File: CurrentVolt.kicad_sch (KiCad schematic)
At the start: 6 parts, among them U13 ACS70331EOLCTR-2P5U3, U14 Opamp_Dual

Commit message: finalising diagram
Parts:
- removed R24, R25: R, symbol Device:R
- removed U14: Opamp_Dual, symbol Device:Opamp_Dual
- renumbered R14 to R22, R15 to R23, U13 to U14
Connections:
- net +3.3V renamed 3v3
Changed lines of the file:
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@@
 (kicad_sch (version 20211123) (generator eeschema)
   (paper "A4")
-  (junction (at 171.45 110.49) (diameter 0) (color 0 0 0 0)
-  )
-  (junction (at 116.84 96.52) (diameter 0) (color 0 0 0 0)
+  (junction (at 116.84 91.44) (diameter 0) (color 0 0 0 0)
   )
   (junction (at 116.84 105.41) (diameter 0) (color 0 0 0 0)
-  )
-  (junction (at 156.21 113.03) (diameter 0) (color 0 0 0 0)
   )
   (junction (at 116.84 114.3) (diameter 0) (color 0 0 0 0)
   )
   (junction (at 83.82 81.28) (diameter 0) (color 0 0 0 0)
-  )
-  (junction (at 130.81 105.41) (diameter 0) (color 0 0 0 0)
   )
   (wire (pts (xy 80.01 81.28) (xy 83.82 81.28))
@@
     (stroke (width 0) (type default) (color 0 0 0 0))
   )
-  (wire (pts (xy 82.55 96.52) (xy 86.36 96.52))
+  (wire (pts (xy 116.84 91.44) (xy 116.84 96.52))
     (stroke (width 0) (type default) (color 0 0 0 0))
   )
-  (wire (pts (xy 171.45 110.49) (xy 171.45 120.65))
+  (wire (pts (xy 71.12 96.52) (xy 86.36 96.52))
     (stroke (width 0) (type default) (color 0 0 0 0))
   )
@@
     (stroke (width 0) (type default) (color 0 0 0 0))
   )
-  (wire (pts (xy 116.84 91.44) (xy 116.84 96.52))
-    (stroke (width 0) (type default) (color 0 0 0 0))
-  )
-  (wire (pts (xy 130.81 105.41) (xy 130.81 129.54))
-    (stroke (width 0) (type default) (color 0 0 0 0))
-  )
-  (wire (pts (xy 116.84 88.9) (xy 133.35 88.9))
-    (stroke (width 0) (type default) (color 0 0 0 0))
-  )
   (wire (pts (xy 71.12 91.44) (xy 86.36 91.44))
-    (stroke (width 0) (type default) (color 0 0 0 0))
-  )
-  (wire (pts (xy 130.81 105.41) (xy 156.21 105.41))
     (stroke (width 0) (type default) (color 0 0 0 0))
   )
@@
     (stroke (width 0) (type default) (color 0 0 0 0))
   )
-  (wire (pts (xy 163.83 120.65) (xy 156.21 120.65))
-    (stroke (width 0) (type default) (color 0 0 0 0))
-  )
-  (wire (pts (xy 171.45 107.95) (xy 171.45 110.49))
-    (stroke (width 0) (type default) (color 0 0 0 0))
-  )
-  (wire (pts (xy 116.84 105.41) (xy 130.81 105.41))
-    (stroke (width 0) (type default) (color 0 0 0 0))
-  )
-  (wire (pts (xy 156.21 120.65) (xy 156.21 113.03))
+  (wire (pts (xy 116.84 105.41) (xy 162.56 105.41))
     (stroke (width 0) (type default) (color 0 0 0 0))
   )
@@
     (stroke (width 0) (type default) (color 0 0 0 0))
   )
-  (wire (pts (xy 116.84 96.52) (xy 162.56 96.52))
-    (stroke (width 0) (type default) (color 0 0 0 0))
-  )
-  (wire (pts (xy 130.81 129.54) (xy 171.45 129.54))
-    (stroke (width 0) (type default) (color 0 0 0 0))
-  )
-  (wire (pts (xy 156.21 110.49) (xy 156.21 113.03))
-    (stroke (width 0) (type default) (color 0 0 0 0))
-  )
-  (wire (pts (xy 142.24 113.03) (xy 148.59 113.03))
+  (wire (pts (xy 116.84 91.44) (xy 162.56 91.44))
     (stroke (width 0) (type default) (color 0 0 0 0))
   )
@@
     (stroke (width 0) (type default) (color 0 0 0 0))
   )
-  (wire (pts (xy 171.45 110.49) (xy 173.99 110.49))
-    (stroke (width 0) (type default) (color 0 0 0 0))
-  )
   (wire (pts (xy 116.84 107.95) (xy 116.84 105.41))
     (stroke (width 0) (type default) (color 0 0 0 0))
   )
-  (wire (pts (xy 133.35 78.74) (xy 133.35 88.9))
+  (wire (pts (xy 116.84 88.9) (xy 162.56 88.9))
     (stroke (width 0) (type default) (color 0 0 0 0))
   )
-  (label "GND_0" (at 116.84 115.57 270)
+  (label "GND" (at 116.84 115.57 270)
     (effects (font (size 1.27 1.27)) (justify right bottom))
   )
-  (label "GND_0" (at 80.01 81.28 180)
+  (label "GND" (at 80.01 81.28 180)
     (effects (font (size 1.27 1.27)) (justify right bottom))
   )
-  (label "GND_0" (at 142.24 113.03 180)
-    (effects (font (size 1.27 1.27)) (justify right bottom))
+  (hierarchical_label "3v3" (shape input) (at 71.12 96.52 180)
+    (effects (font (size 1.27 1.27)) (justify right))
   )
   (hierarchical_label "GND" (shape input) (at 66.04 114.3 180)
     (effects (font (size 1.27 1.27)) (justify right))
   )
-  (hierarchical_label "Vin" (shape input) (at 133.35 78.74 90)
+  (hierarchical_label "Vin" (shape input) (at 162.56 88.9 0)
     (effects (font (size 1.27 1.27)) (justify left))
   )
-  (hierarchical_label "Vinv" (shape input) (at 173.99 110.49 0)
+  (hierarchical_label "Vsense" (shape input) (at 162.56 105.41 0)
     (effects (font (size 1.27 1.27)) (justify left))
   )
@@
     (effects (font (size 1.27 1.27)) (justify right))
   )
-  (hierarchical_label "Vsense" (shape input) (at 171.45 129.54 0)
+  (hierarchical_label "Out V" (shape input) (at 162.56 91.44 0)
     (effects (font (size 1.27 1.27)) (justify left))
-  )
-  (hierarchical_label "Out V" (shape input) (at 162.56 96.52 0)
-    (effects (font (size 1.27 1.27)) (justify left))
-  )
-  (symbol (lib_id "Device:Opamp_Dual") (at 163.83 107.95 0) (mirror x) (unit 1)
-    (in_bom yes) (on_board yes) (fields_autoplaced)
-    (property "Reference" "U14" (id 0) (at 163.83 99.1702 0))
-    (property "Value" "Opamp_Dual" (id 1) (at 163.83 101.7071 0))
-    (property "Footprint" "" (id 2) (at 163.83 107.95 0)
-      (effects (font (size 1.27 1.27)) hide)
-    )
-    (property "Datasheet" "~" (id 3) (at 163.83 107.95 0)
-      (effects (font (size 1.27 1.27)) hide)
-    )
-    (pin "1")
-    (pin "2")
-    (pin "3")
-    (pin "5")
-    (pin "6")
-    (pin "7")
-    (pin "4")
-    (pin "8")
   )
   (symbol (lib_id "Device:R_Small") (at 116.84 99.06 0) (unit 1)
     (in_bom yes) (on_board yes) (fields_autoplaced)
-    (property "Reference" "R14" (id 0) (at 118.3386 98.2253 0)
+    (property "Reference" "R22" (id 0) (at 118.3386 98.2253 0)
       (effects (font (size 1.27 1.27)) (justify left))
     )
@@
     (pin "2")
   )
-  (symbol (lib_id "Device:R") (at 152.4 113.03 90) (unit 1)
+  (symbol (lib_id "power:PWR_FLAG") (at 83.82 81.28 0) (unit 1)
     (in_bom yes) (on_board yes) (fields_autoplaced)
-    (property "Reference" "R24" (id 0) (at 152.4 108.3142 90))
-    (property "Value" "R" (id 1) (at 152.4 110.8511 90))
-    (property "Footprint" "" (id 2) (at 152.4 114.808 90)
+    (property "Reference" "#FLG08" (id 0) (at 83.82 79.375 0)
       (effects (font (size 1.27 1.27)) hide)
     )
-    (property "Datasheet" "~" (id 3) (at 152.4 113.03 0)
+    (property "Value" "PWR_FLAG" (id 1) (at 83.82 77.7042 0)
       (effects (font (size 1.27 1.27)) hide)
     )
-    (pin "1")
-    (pin "2")
-  )
-  (symbol (lib_id "power:+3.3V") (at 82.55 96.52 90) (unit 1)
-    (in_bom yes) (on_board yes) (fields_autoplaced)
-    (property "Reference" "#PWR0114" (id 0) (at 86.36 96.52 0)
-      (effects (font (size 1.27 1.27)) hide)
-    )
-    (property "Value" "+3.3V" (id 1) (at 79.375 96.9538 90)
-      (effects (font (size 1.27 1.27)) (justify left))
-    )
-    (property "Footprint" "" (id 2) (at 82.55 96.52 0)
-      (effects (font (size 1.27 1.27)) hide)
-    )
-    (property "Datasheet" "" (id 3) (at 82.55 96.52 0)
-      (effects (font (size 1.27 1.27)) hide)
-    )
-    (pin "1")
-  )
-  (symbol (lib_id "power:PWR_FLAG") (at 83.82 81.28 0) (unit 1)
-    (in_bom yes) (on_board yes) (fields_autoplaced)
-    (property "Reference" "#FLG0106" (id 0) (at 83.82 79.375 0)
-      (effects (font (size 1.27 1.27)) hide)
-    )
-    (property "Value" "PWR_FLAG" (id 1) (at 83.82 77.7042 0))
     (property "Footprint" "" (id 2) (at 83.82 81.28 0)
       (effects (font (size 1.27 1.27)) hide)
@@
   (symbol (lib_id "ACS70331EOLCTR-2P5U3:ACS70331EOLCTR-2P5U3") (at 101.6 88.9 180) (unit 1)
     (in_bom yes) (on_board yes)
-    (property "Reference" "U13" (id 0) (at 101.6 75.0402 0))
+    (property "Reference" "U14" (id 0) (at 101.6 75.0402 0))
     (property "Value" "ACS70331EOLCTR-2P5U3" (id 1) (at 101.6 72.39 0))
     (property "Footprint" "SOIC127P600X175-8N" (id 2) (at 101.6 88.9 0)
@@
   (symbol (lib_id "Device:R_Small") (at 116.84 110.49 0) (unit 1)
     (in_bom yes) (on_board yes) (fields_autoplaced)
-    (property "Reference" "R15" (id 0) (at 118.3386 109.6553 0)
+    (property "Reference" "R23" (id 0) (at 118.3386 109.6553 0)
       (effects (font (size 1.27 1.27)) (justify left))
     )
@@
       (effects (font (size 1.27 1.27)) hide)
     )
-    (pin "1")
-    (pin "2")
-  )
-  (symbol (lib_id "Device:R") (at 167.64 120.65 90) (unit 1)
-    (in_bom yes) (on_board yes) (fields_autoplaced)
-    (property "Reference" "R25" (id 0) (at 167.64 115.9342 90))
-    (property "Value" "R" (id 1) (at 167.64 118.4711 90))
-    (property "Footprint" "" (id 2) (at 167.64 122.428 90)
-      (effects (font (size 1.27 1.27)) hide)
-    )
-    (property "Datasheet" "~" (id 3) (at 167.64 120.65 0)
-      (effects (font (size 1.27 1.27)) hide)
-    )

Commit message: last TH mounting board
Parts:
- added C36, C37, C38: 0.1uF, Capacitor_SMD:C_0603_1608Metric, symbol Device:C_Small
- R16: renamed from R22; value R_Small -> 20k; footprint Resistor_THT:R_Axial_DIN0207_L6.3mm_D2.5mm_P5.08mm_Vertical -> Resistor_SMD:R_0603_1608Metric
- R17: renamed from R23; value R_Small -> 10k; footprint Resistor_THT:R_Axial_DIN0207_L6.3mm_D2.5mm_P5.08mm_Vertical -> Resistor_SMD:R_0603_1608Metric
- U10: renamed from U14; footprint SOIC127P600X175-8N -> ACS70331EOLCTR-2P5U3:SOIC127P600X175-8N
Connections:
- net 3v3: now also C37.1
- net GND: now also C36.1, C37.2, C38.2
- net Isense: now also C36.2
- net Vsense: now also C38.1
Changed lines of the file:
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@@
 (kicad_sch (version 20211123) (generator eeschema)
   (paper "A4")
+  (junction (at 133.604 105.41) (diameter 0) (color 0 0 0 0)
+  )
   (junction (at 116.84 91.44) (diameter 0) (color 0 0 0 0)
   )
@@
   (junction (at 116.84 114.3) (diameter 0) (color 0 0 0 0)
   )
-  (junction (at 83.82 81.28) (diameter 0) (color 0 0 0 0)
-  )
-  (wire (pts (xy 80.01 81.28) (xy 83.82 81.28))
-    (stroke (width 0) (type default) (color 0 0 0 0))
-  )
-  (wire (pts (xy 83.82 81.28) (xy 86.36 81.28))
+  (junction (at 81.28 81.28) (diameter 0) (color 0 0 0 0)
+  )
+  (junction (at 78.232 96.52) (diameter 0) (color 0 0 0 0)
+  )
+  (junction (at 81.28 91.44) (diameter 0) (color 0 0 0 0)
+  )
+  (wire (pts (xy 80.01 81.28) (xy 81.28 81.28))
+    (stroke (width 0) (type default) (color 0 0 0 0))
+  )
+  (wire (pts (xy 133.604 114.3) (xy 133.604 110.49))
     (stroke (width 0) (type default) (color 0 0 0 0))
   )
@@
     (stroke (width 0) (type default) (color 0 0 0 0))
   )
-  (wire (pts (xy 71.12 96.52) (xy 86.36 96.52))
+  (wire (pts (xy 71.12 96.52) (xy 78.232 96.52))
     (stroke (width 0) (type default) (color 0 0 0 0))
   )
@@
     (stroke (width 0) (type default) (color 0 0 0 0))
   )
-  (wire (pts (xy 71.12 91.44) (xy 86.36 91.44))
+  (wire (pts (xy 71.12 91.44) (xy 81.28 91.44))
+    (stroke (width 0) (type default) (color 0 0 0 0))
+  )
+  (wire (pts (xy 81.28 91.44) (xy 86.36 91.44))
+    (stroke (width 0) (type default) (color 0 0 0 0))
+  )
+  (wire (pts (xy 78.232 96.52) (xy 86.36 96.52))
     (stroke (width 0) (type default) (color 0 0 0 0))
   )
@@
     (stroke (width 0) (type default) (color 0 0 0 0))
   )
-  (wire (pts (xy 116.84 105.41) (xy 162.56 105.41))
+  (wire (pts (xy 116.84 105.41) (xy 133.604 105.41))
+    (stroke (width 0) (type default) (color 0 0 0 0))
+  )
+  (wire (pts (xy 81.28 81.28) (xy 86.36 81.28))
+    (stroke (width 0) (type default) (color 0 0 0 0))
+  )
+  (wire (pts (xy 116.84 114.3) (xy 133.604 114.3))
     (stroke (width 0) (type default) (color 0 0 0 0))
   )
@@
     (stroke (width 0) (type default) (color 0 0 0 0))
   )
+  (wire (pts (xy 133.604 105.41) (xy 162.56 105.41))
+    (stroke (width 0) (type default) (color 0 0 0 0))
+  )
   (wire (pts (xy 116.84 115.57) (xy 116.84 114.3))
+    (stroke (width 0) (type default) (color 0 0 0 0))
+  )
+  (wire (pts (xy 81.28 81.28) (xy 81.28 86.36))
     (stroke (width 0) (type default) (color 0 0 0 0))
   )
@@
     (effects (font (size 1.27 1.27)) (justify right bottom))
   )
+  (label "GND" (at 78.232 101.6 270)
+    (effects (font (size 1.27 1.27)) (justify right bottom))
+  )
   (label "GND" (at 80.01 81.28 180)
     (effects (font (size 1.27 1.27)) (justify right bottom))
@@
   (symbol (lib_id "Device:R_Small") (at 116.84 99.06 0) (unit 1)
     (in_bom yes) (on_board yes) (fields_autoplaced)
-    (property "Reference" "R22" (id 0) (at 118.3386 98.2253 0)
-      (effects (font (size 1.27 1.27)) (justify left))
-    )
-    (property "Value" "R_Small" (id 1) (at 118.3386 100.7622 0)
-      (effects (font (size 1.27 1.27)) (justify left))
-    )
-    (property "Footprint" "Resistor_THT:R_Axial_DIN0207_L6.3mm_D2.5mm_P5.08mm_Vertical" (id 2) (at 116.84 99.06 0)
+    (property "Reference" "R16" (id 0) (at 118.3386 98.2253 0)
+      (effects (font (size 1.27 1.27)) (justify left))
+    )
+    (property "Value" "20k" (id 1) (at 118.3386 100.7622 0)
+      (effects (font (size 1.27 1.27)) (justify left))
+    )
+    (property "Footprint" "Resistor_SMD:R_0603_1608Metric" (id 2) (at 116.84 99.06 0)
       (effects (font (size 1.27 1.27)) hide)
     )
@@
     (pin "2")
   )
-  (symbol (lib_id "power:PWR_FLAG") (at 83.82 81.28 0) (unit 1)
-    (in_bom yes) (on_board yes) (fields_autoplaced)
-    (property "Reference" "#FLG08" (id 0) (at 83.82 79.375 0)
-      (effects (font (size 1.27 1.27)) hide)
-    )
-    (property "Value" "PWR_FLAG" (id 1) (at 83.82 77.7042 0)
-      (effects (font (size 1.27 1.27)) hide)
-    )
-    (property "Footprint" "" (id 2) (at 83.82 81.28 0)
-      (effects (font (size 1.27 1.27)) hide)
-    )
-    (property "Datasheet" "~" (id 3) (at 83.82 81.28 0)
-      (effects (font (size 1.27 1.27)) hide)
-    )
-    (pin "1")
+  (symbol (lib_id "Device:C_Small") (at 78.232 99.06 0) (unit 1)
+    (in_bom yes) (on_board yes) (fields_autoplaced)
+    (property "Reference" "C37" (id 0) (at 80.5561 98.2316 0)
+      (effects (font (size 1.27 1.27)) (justify left))
+    )
+    (property "Value" "0.1uF" (id 1) (at 80.5561 100.7685 0)
+      (effects (font (size 1.27 1.27)) (justify left))
+    )
+    (property "Footprint" "Capacitor_SMD:C_0603_1608Metric" (id 2) (at 78.232 99.06 0)
+      (effects (font (size 1.27 1.27)) hide)
+    )
+    (property "Datasheet" "~" (id 3) (at 78.232 99.06 0)
+      (effects (font (size 1.27 1.27)) hide)
+    )
+    (pin "1")
+    (pin "2")
   )
   (symbol (lib_id "ACS70331EOLCTR-2P5U3:ACS70331EOLCTR-2P5U3") (at 101.6 88.9 180) (unit 1)
     (in_bom yes) (on_board yes)
-    (property "Reference" "U14" (id 0) (at 101.6 75.0402 0))
+    (property "Reference" "U10" (id 0) (at 101.6 75.0402 0))
     (property "Value" "ACS70331EOLCTR-2P5U3" (id 1) (at 101.6 72.39 0))
-    (property "Footprint" "SOIC127P600X175-8N" (id 2) (at 101.6 88.9 0)
+    (property "Footprint" "ACS70331EOLCTR-2P5U3:SOIC127P600X175-8N" (id 2) (at 101.6 88.9 0)
       (effects (font (size 1.27 1.27)) (justify left bottom) hide)
     )
@@
     (pin "8")
   )
+  (symbol (lib_id "Device:C_Small") (at 81.28 88.9 0) (unit 1)
+    (in_bom yes) (on_board yes) (fields_autoplaced)
+    (property "Reference" "C36" (id 0) (at 83.6041 88.0716 0)
+      (effects (font (size 1.27 1.27)) (justify left))
+    )
+    (property "Value" "0.1uF" (id 1) (at 83.6041 90.6085 0)
+      (effects (font (size 1.27 1.27)) (justify left))
+    )
+    (property "Footprint" "Capacitor_SMD:C_0603_1608Metric" (id 2) (at 81.28 88.9 0)
+      (effects (font (size 1.27 1.27)) hide)
+    )
+    (property "Datasheet" "~" (id 3) (at 81.28 88.9 0)
+      (effects (font (size 1.27 1.27)) hide)
+    )
+    (pin "1")
+    (pin "2")
+  )
   (symbol (lib_id "Device:R_Small") (at 116.84 110.49 0) (unit 1)
     (in_bom yes) (on_board yes) (fields_autoplaced)
-    (property "Reference" "R23" (id 0) (at 118.3386 109.6553 0)
-      (effects (font (size 1.27 1.27)) (justify left))
-    )
-    (property "Value" "R_Small" (id 1) (at 118.3386 112.1922 0)
-      (effects (font (size 1.27 1.27)) (justify left))
-    )
-    (property "Footprint" "Resistor_THT:R_Axial_DIN0207_L6.3mm_D2.5mm_P5.08mm_Vertical" (id 2) (at 116.84 110.49 0)
+    (property "Reference" "R17" (id 0) (at 118.3386 109.6553 0)
+      (effects (font (size 1.27 1.27)) (justify left))
+    )
+    (property "Value" "10k" (id 1) (at 118.3386 112.1922 0)
+      (effects (font (size 1.27 1.27)) (justify left))
+    )
+    (property "Footprint" "Resistor_SMD:R_0603_1608Metric" (id 2) (at 116.84 110.49 0)
       (effects (font (size 1.27 1.27)) hide)
     )
@@
       (effects (font (size 1.27 1.27)) hide)
     )
+    (pin "1")
+    (pin "2")
+  )
+  (symbol (lib_id "Device:C_Small") (at 133.604 107.95 0) (unit 1)
+    (in_bom yes) (on_board yes) (fields_autoplaced)
+    (property "Reference" "C38" (id 0) (at 135.9281 107.1216 0)
+      (effects (font (size 1.27 1.27)) (justify left))
+    )
+    (property "Value" "0.1uF" (id 1) (at 135.9281 109.6585 0)
+      (effects (font (size 1.27 1.27)) (justify left))
+    )
+    (property "Footprint" "Capacitor_SMD:C_0603_1608Metric" (id 2) (at 133.604 107.95 0)
+      (effects (font (size 1.27 1.27)) hide)
+    )
+    (property "Datasheet" "~" (id 3) (at 133.604 107.95 0)
+      (effects (font (size 1.27 1.27)) hide)
+    )

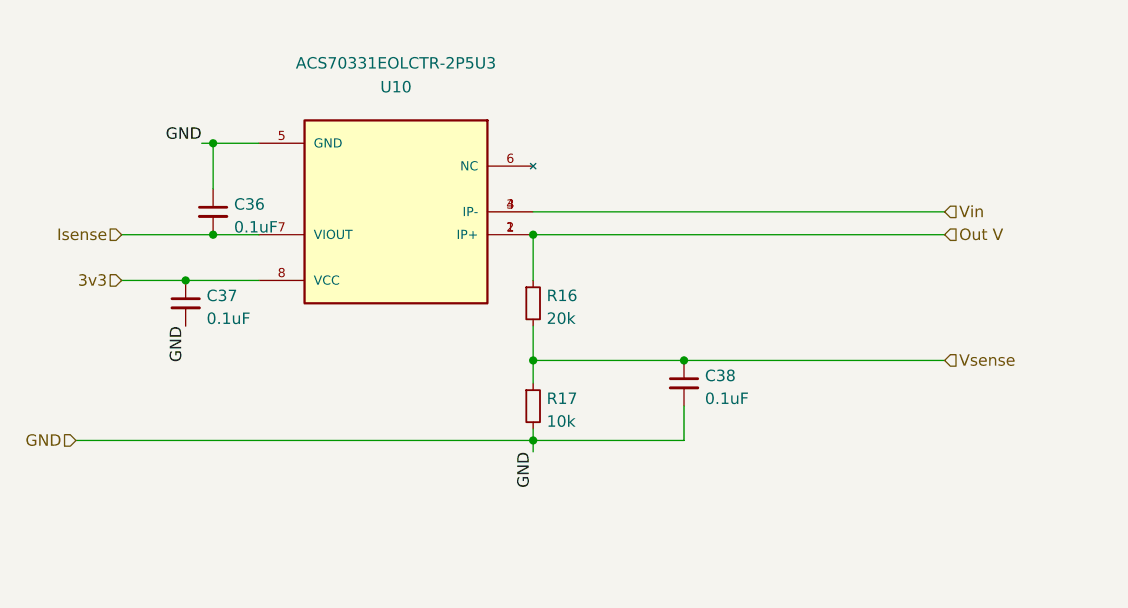
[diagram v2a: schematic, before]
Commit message: all SMD components going into boards
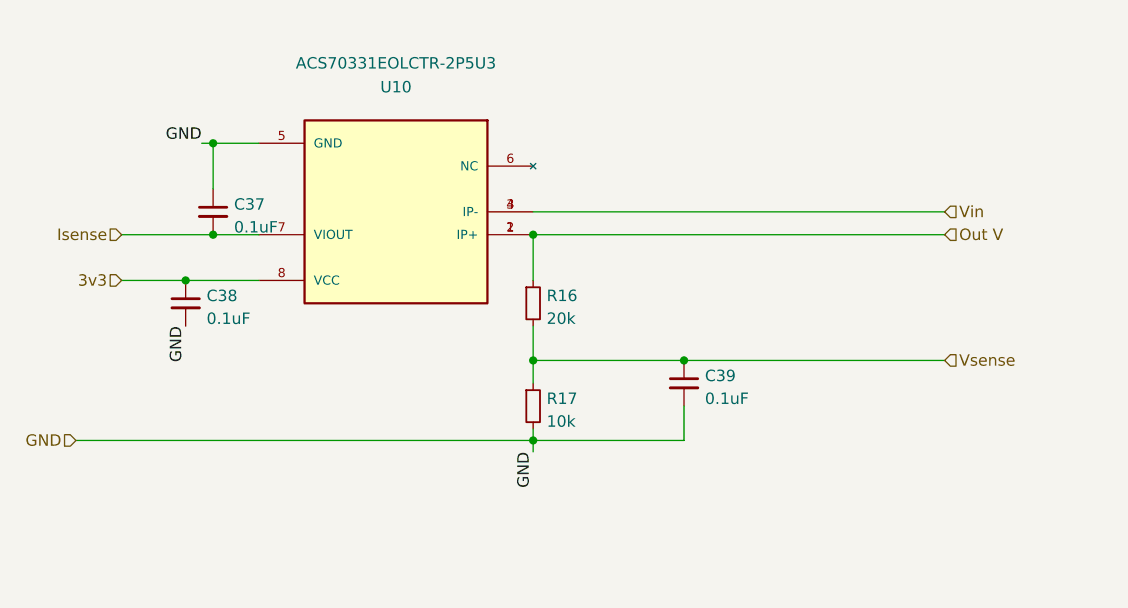
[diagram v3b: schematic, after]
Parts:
- renumbered C36 to C37, C37 to C38, C38 to C39
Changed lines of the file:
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@@
   (symbol (lib_id "Device:C_Small") (at 78.232 99.06 0) (unit 1)
     (in_bom yes) (on_board yes) (fields_autoplaced)
-    (property "Reference" "C37" (id 0) (at 80.5561 98.2316 0)
+    (property "Reference" "C38" (id 0) (at 80.5561 98.2316 0)
       (effects (font (size 1.27 1.27)) (justify left))
     )
@@
   (symbol (lib_id "Device:C_Small") (at 81.28 88.9 0) (unit 1)
     (in_bom yes) (on_board yes) (fields_autoplaced)
-    (property "Reference" "C36" (id 0) (at 83.6041 88.0716 0)
+    (property "Reference" "C37" (id 0) (at 83.6041 88.0716 0)
       (effects (font (size 1.27 1.27)) (justify left))
     )
@@
   (symbol (lib_id "Device:C_Small") (at 133.604 107.95 0) (unit 1)
     (in_bom yes) (on_board yes) (fields_autoplaced)
-    (property "Reference" "C38" (id 0) (at 135.9281 107.1216 0)
+    (property "Reference" "C39" (id 0) (at 135.9281 107.1216 0)
       (effects (font (size 1.27 1.27)) (justify left))
     )
